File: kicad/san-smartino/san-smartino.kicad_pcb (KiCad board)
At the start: 2 copper layers, 69.9 x 54.6 mm, 47 parts, among them J1 GND CTS VBUS RX TX DTR, J2 SDA SCL -3V3 GND, J3 Conn_01x07_Male, SW1 Reset, SW2 Flash, U1 BQ27441DRZR-G1A, U2 ESP-12E, U3 LTC3440

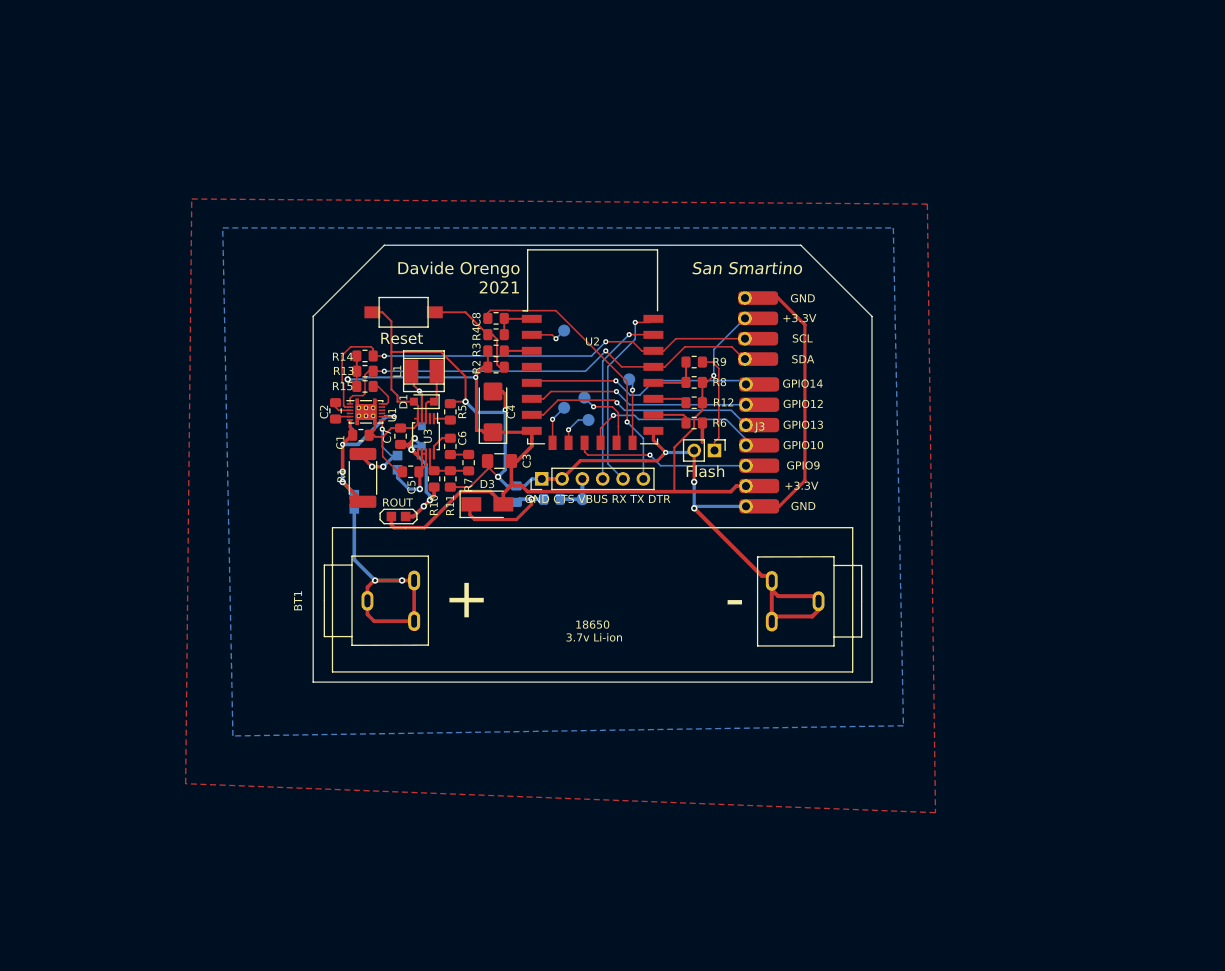
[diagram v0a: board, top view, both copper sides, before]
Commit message: schematic updated, second battery and edgecut
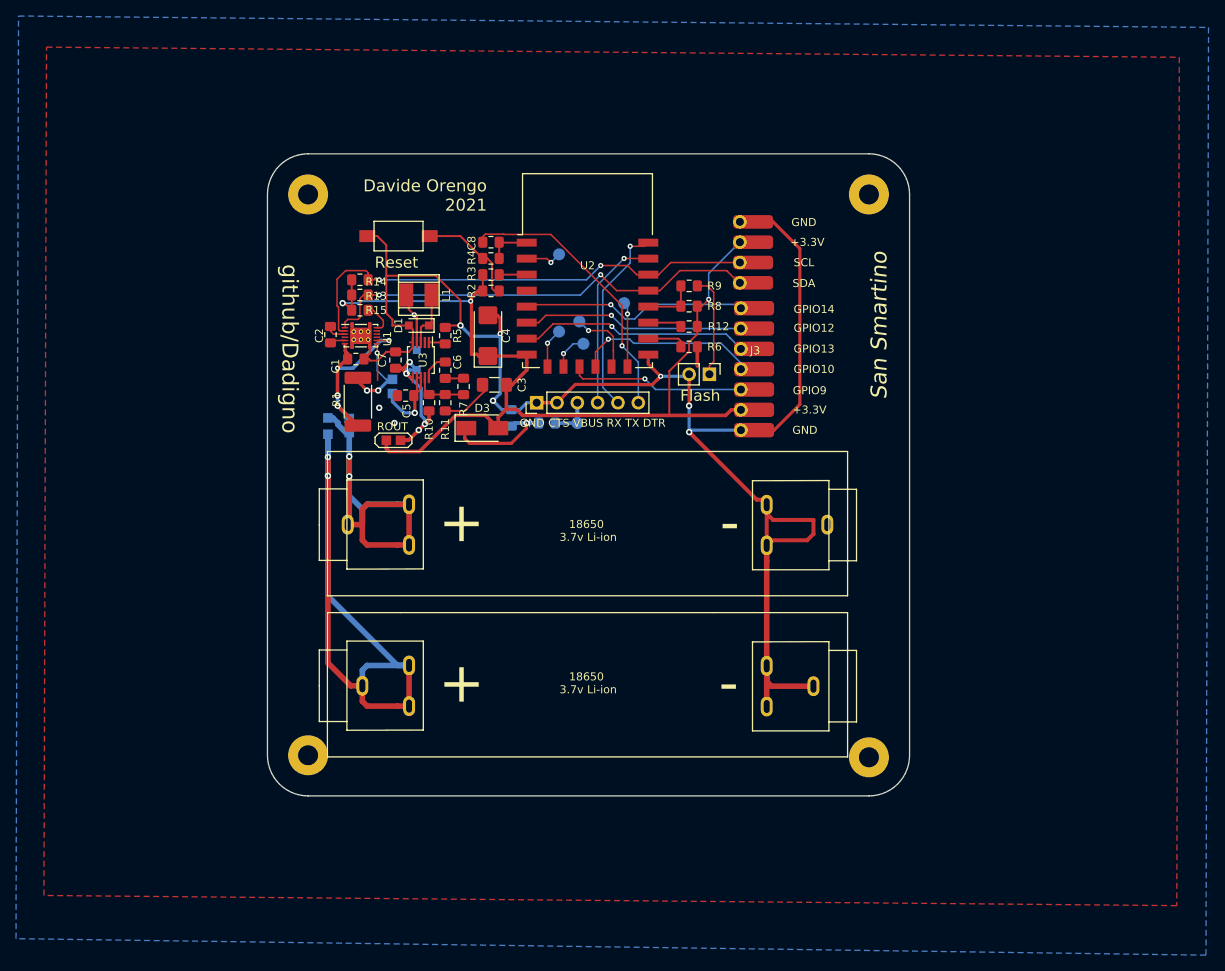
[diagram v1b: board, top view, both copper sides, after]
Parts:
- added BT2: 2.45v-4.5v, san-smartino:18650-battery-metal-clips, F.Cu at (74.8, 88.1)
- added REF**: MountingHole_2.5mm_Pad, MountingHole:MountingHole_2.5mm_Pad, F.Cu at (73.7, 96.8)
- added REF**: MountingHole_2.5mm_Pad, MountingHole:MountingHole_2.5mm_Pad, F.Cu at (73.7, 26.7)
- added REF**: MountingHole_2.5mm_Pad, MountingHole:MountingHole_2.5mm_Pad, F.Cu at (143.8, 26.7)
- added REF**: MountingHole_2.5mm_Pad, MountingHole:MountingHole_2.5mm_Pad, F.Cu at (143.8, 97.0)
- added TP10: BATT_2, TestPoint:TestPoint_2Pads_Pitch2.54mm_Drill0.8mm, B.Cu at (76.1, 56.9)
- TP9: value BATT -> BATT_1
- moved BT1 9.55 mm to (74.8, 67.9)
- moved D1 9.55 mm to (87.5, 43.1)
- moved TP2 9.55 mm to (84.2, 51.9)
- moved TP4 9.55 mm to (105.0, 34.2)
- moved TP5 9.55 mm to (105.0, 43.8)
- moved R17 9.55 mm to (99.1, 54.6)
- moved J2 9.55 mm to (127.6, 30.1)
- moved SW1 9.55 mm to (85.0, 31.9)
- moved C2 9.55 mm to (76.5, 44.2)
- moved C4 9.55 mm to (96.1, 44.3)
- moved C7 9.55 mm to (84.6, 47.4)
- moved C8 9.55 mm to (96.5, 32.6)
- moved D2 9.55 mm to (87.2, 47.4)
- moved J1 9.55 mm to (102.2, 52.7)
- moved L1 9.55 mm to (87.5, 39.2)
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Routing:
- net Net-(BT2-Pad1): track 0.00 -> 91.5 mm, vias 0 -> 2
- net -BATT: track 200.1 -> 224.1 mm, vias 6 -> 8
- net Net-(BT1-Pad1): track 34.4 -> 53.0 mm
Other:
- board size 69.9 x 54.6 mm -> 80.3 x 80.3 mm
- board text added: "github/Dadigno"

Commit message: updated board
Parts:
- removed BT2: 2.45v-4.5v, san-smartino:18650-battery-metal-clips
- removed REF** (x4): MountingHole_2.5mm_Pad, MountingHole:MountingHole_2.5mm_Pad
- added C10: 100nF, Capacitor_SMD:C_0805_2012Metric_Pad1.15x1.40mm_HandSolder, F.Cu at (82.5, 64.0)
- added C11: 10uF, Capacitor_SMD:C_0805_2012Metric_Pad1.15x1.40mm_HandSolder, F.Cu at (97.3, 60.7)
- added C9: 0.1uF, Capacitor_SMD:C_0805_2012Metric_Pad1.15x1.40mm_HandSolder, F.Cu at (108.8, 64.5)
- added D4: STDBY, LED_SMD:LED_0603_1608Metric_Pad1.05x0.95mm_HandSolder, F.Cu at (104.3, 63.9)
- added D5: CHRG, LED_SMD:LED_0603_1608Metric_Pad1.05x0.95mm_HandSolder, F.Cu at (101.1, 63.9)
- added H1: MountingHole, MountingHole:MountingHole_3.2mm_M3_Pad_Via, F.Cu at (73.0, 26.8)
- added H2: MountingHole, MountingHole:MountingHole_3.2mm_M3_Pad_Via, F.Cu at (73.0, 87.0)
- added H3: MountingHole, MountingHole:MountingHole_3.2mm_M3_Pad_Via, F.Cu at (143.1, 26.8)
- added H4: MountingHole, MountingHole:MountingHole_3.2mm_M3_Pad_Via, F.Cu at (143.0, 87.0)
- added J4: CHRG IN, Connector_PinHeader_2.54mm:PinHeader_1x02_P2.54mm_Vertical, F.Cu at (128.8, 63.0)
- added J5: PW-SEL, Connector_PinHeader_2.54mm:PinHeader_1x03_P2.54mm_Vertical, B.Cu at (75.9, 55.2)
- added R18: 1.2k, Resistor_SMD:R_0805_2012Metric_Pad1.15x1.40mm_HandSolder, F.Cu at (119.5, 59.6)
- added R19: 1k, Resistor_SMD:R_0805_2012Metric_Pad1.15x1.40mm_HandSolder, F.Cu at (104.3, 60.1)
- added R20: 1k, Resistor_SMD:R_0805_2012Metric_Pad1.15x1.40mm_HandSolder, F.Cu at (101.1, 60.1)
- added R21: 1k, Resistor_SMD:R_0805_2012Metric_Pad1.15x1.40mm_HandSolder, F.Cu at (90.8, 61.2)
- added R22: 100R, Resistor_SMD:R_0805_2012Metric_Pad1.15x1.40mm_HandSolder, F.Cu at (80.4, 60.7)
- added U4: TP4056, Package_SO:SOP-8-1EP_4.57x4.57mm_P1.27mm_EP4.57x4.45mm, F.Cu at (111.4, 60.1)
- added U5: DW01, Package_TO_SOT_SMD:SOT-23-6_Handsoldering, F.Cu at (86.5, 64.2)
- added U6: FS8205A, Package_SO:TSSOP-8_4.4x3mm_P0.65mm, F.Cu at (94.6, 64.3)
- SW1: footprint Button_Switch_SMD:SW_SPST_CK_RS282G05A3 -> Button_Switch_SMD:SW_SPST_EVQP0
- TP10: value BATT_2 -> Wake; footprint TestPoint:TestPoint_2Pads_Pitch2.54mm_Drill0.8mm -> TestPoint:TestPoint_Pad_D1.5mm
- TP9: value BATT_1 -> BATT; moved to F.Cu
- moved TP10 35.5 mm to (105.9, 37.6), turned to 0 degrees
- moved BT1 7.51 mm to (74.3, 75.4)
- moved TP9 5.82 mm to (76.3, 62.1)
- moved SW1 1.90 mm to (83.4, 30.7)
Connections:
- net +BATT renamed VCC
- net /BIN renamed Net-(U1-Pad10)
- BT1 pad 2: -BATT -> BATT-
- C1 pad 1: Net-(C1-Pad1) -> FUEL-GAUGE
- C1 pad 2: -BATT -> IN-
- C2 pad 2: -BATT -> IN-
- C3 pad 2: -BATT -> IN-
- C4 pad 2: -BATT -> IN-
- C5 pad 2: -BATT -> IN-
- C7 pad 2: -BATT -> IN-
- D1 pad 2: -BATT -> IN-
- J1 pad 1: -BATT -> IN-
- J1 pad 2: -BATT -> IN-
- J2 pad 1: -BATT -> IN-
- J3 pad 7: -BATT -> IN-
- R1 pad 1: Net-(C1-Pad1) -> FUEL-GAUGE
- R11 pad 2: -BATT -> IN-
- R17 pad 2: -BATT -> IN-
- R5 pad 2: -BATT -> IN-
- R6 pad 2: -BATT -> IN-
- SW1 pad 1: -BATT -> IN-
- SW2 pad 2: -BATT -> IN-
- TP10 pad 1: Net-(BT2-Pad1) -> /WAKE
- TP9 pad 2: Net-(C1-Pad1) -> BATT+
- U1 pad 13: -BATT -> IN-
- U1 pad 3: -BATT -> IN-
- U1 pad 6: Net-(C1-Pad1) -> FUEL-GAUGE
- U1 pad 8: Net-(C1-Pad1) -> FUEL-GAUGE
- U2 pad 15: -BATT -> IN-
- U2 pad 4: (no net) -> /WAKE
- U3 pad 5: -BATT -> IN-
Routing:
- net -BATT: track 224.1 -> 0.00 mm, vias 8 -> 0
- net IN-: track 0.00 -> 202.2 mm, vias 0 -> 8
- net Net-(BT2-Pad1): track 91.5 -> 0.00 mm, vias 2 -> 0
- net BATT-: track 0.00 -> 71.3 mm
- net BATT+: track 0.00 -> 46.0 mm, vias 0 -> 1
- net IN+: track 0.00 -> 40.1 mm, vias 0 -> 2
- net Net-(C1-Pad1): track 25.6 -> 0.00 mm, vias 4 -> 0
- net FUEL-GAUGE: track 0.00 -> 23.9 mm, vias 0 -> 3
- net Net-(U5-Pad3): track 0.00 -> 18.5 mm
- net Net-(BT1-Pad1): track 53.0 -> 40.1 mm, vias 2 -> 0
- net VCC: track 12.0 -> 21.6 mm
- net Net-(R2-Pad2): track 13.4 -> 21.7 mm
- net Net-(R20-Pad2): track 0.00 -> 6.82 mm
- net Net-(C10-Pad1): track 0.00 -> 5.79 mm
- net /WAKE: track 0.00 -> 5.39 mm, vias 0 -> 1
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- added copper zone on B.Cu, net IN-
- added copper zone on F.Cu, net IN-
- removed copper zone on B.Cu, net -BATT
- removed copper zone on F.Cu, net -BATT
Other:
- board size 80.3 x 80.3 mm -> 80.5 x 70.6 mm
